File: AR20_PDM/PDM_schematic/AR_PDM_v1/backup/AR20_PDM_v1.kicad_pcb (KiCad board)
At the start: 2 copper layers, 118 x 112 mm, 243 parts, among them J1 S_T_?, J2 1-776163-1, K1 DIPxx-1Cxx-51x, K2 DIPxx-1Cxx-51x, Q1 BTS50025-1TAD, Q10 N_FET, Q11 N_FET, Q12 N_FET, Q13 N_FET, Q14 N_FET, Q15 N_FET, Q16 N_FET, Q17 N_FET, Q18 N_FET, Q2 BTS50025-1TAD, Q3 BTS50025-1TAD, Q4 BTS50025-1TAD, Q5 BTS50025-1TAD, Q6 BTS50025-1TAD, Q7 BTS50025-1TAD, Q8 N_FET, Q9 N_FET, SW1 SW_DIP_x07, SW2 SW_Push, U1 ACM_2020, U10 INA233, U11 INA233, U12 TCA6424ARGJR, U13 Fet-P, U14 Fet-P, U15 Fet-P, U16 Fet-P, U17 Fet-P, U18 Fet-P, U19 Fet-P, U2 INA233, U20 Fet-P, U21 Fet-P, U22 Fet-P, U23 Fet-P, U24 Fet-P, U25 Fet-P, U26 Fet-P, U27 Fet-P, U28 Fet-P, U29 Fet-P, U3 INA233, U30 Fet-P, U31 Fet-P, U4 INA233, U5 INA233, U6 INA233, U7 INA233, U8 INA233, U9 INA233

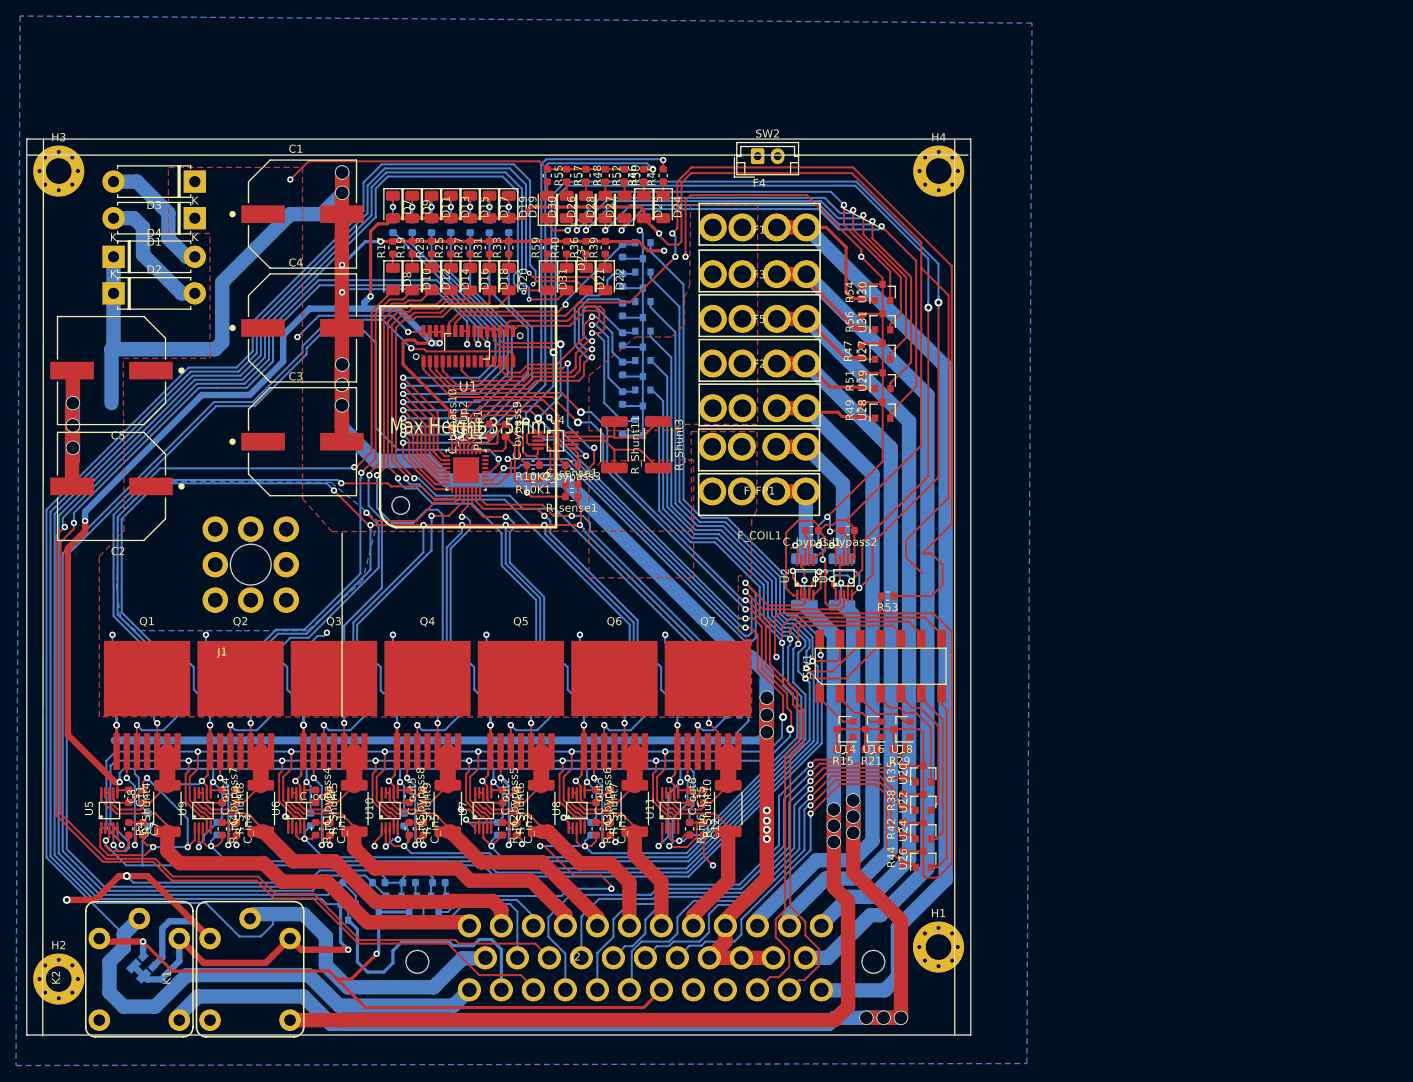
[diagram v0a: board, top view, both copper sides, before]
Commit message: Finilizing the desing, some few missing components
- Increased the size to accommodate mounting holes
- Fixed wrong p mos pin out, due to wrong schematics drawing
- Done alot of tweeeks 
- Button connector still missing.
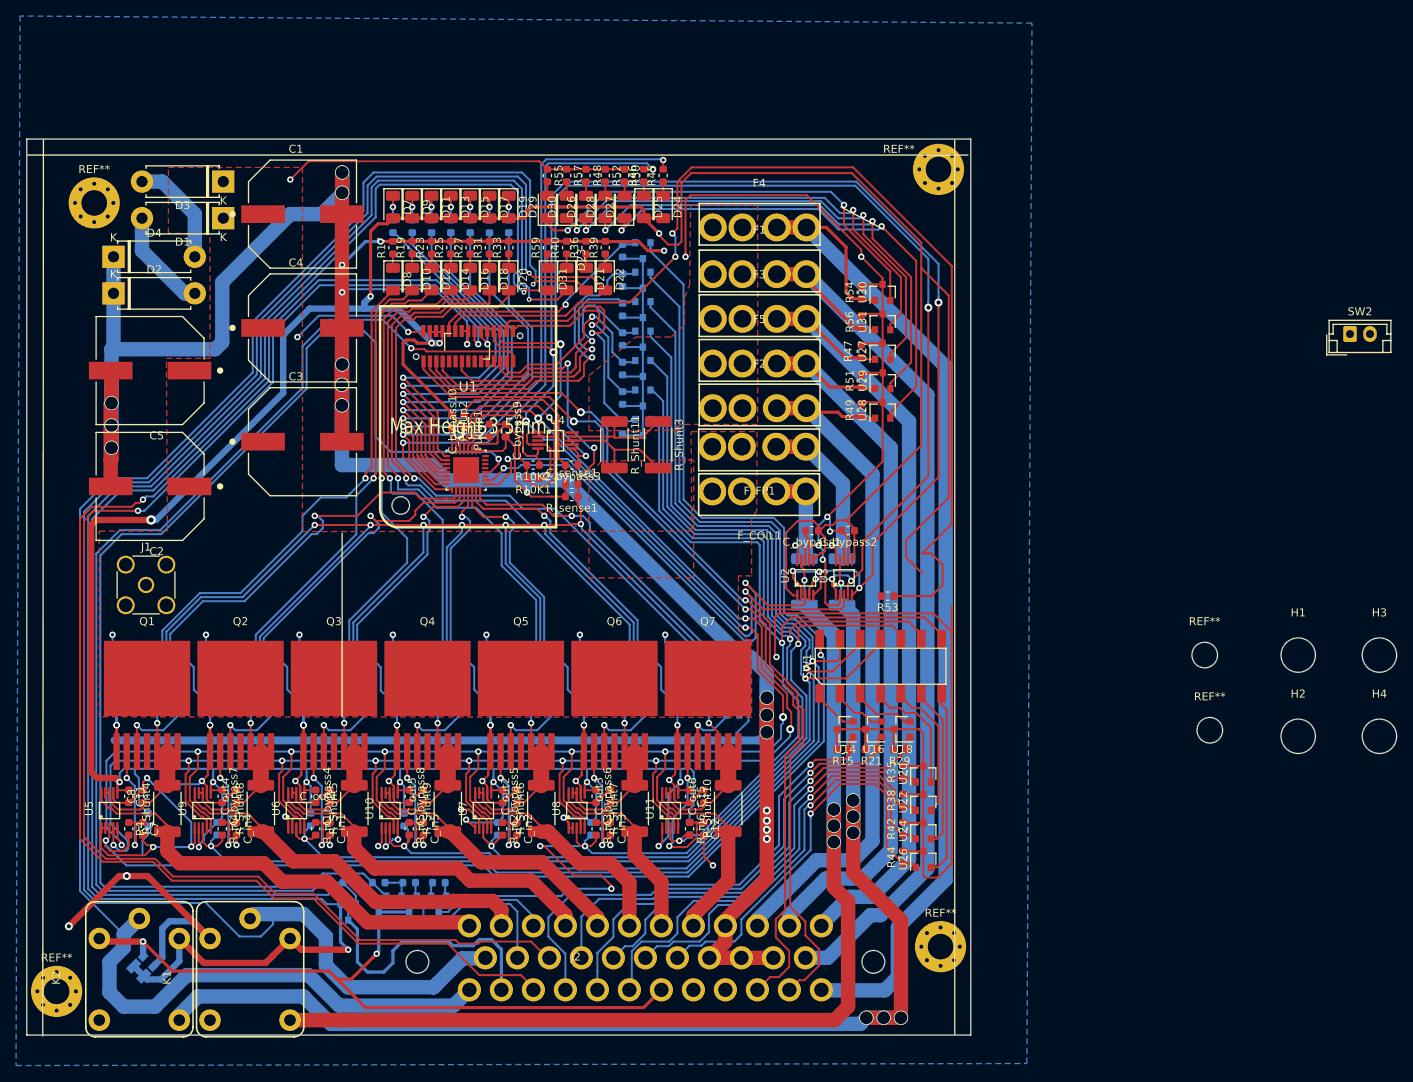
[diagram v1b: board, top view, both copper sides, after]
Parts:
- added REF**: MountingHole_3.2mm_M3_Pad_Via, MountingHole:MountingHole_3.2mm_M3_Pad_Via, F.Cu at (42.3, 44.3)
- added REF**: MountingHole_3.2mm_M3_Pad_Via, MountingHole:MountingHole_3.2mm_M3_Pad_Via, F.Cu at (147.8, 40.1)
- added REF**: MountingHole_3.2mm_M3_Pad_Via, MountingHole:MountingHole_3.2mm_M3_Pad_Via, F.Cu at (148.1, 137.3)
- added REF**: MountingHole_3.2mm_M3_PDM, AR_PDM_v1:MountingHole_3.2mm_M3, F.Cu at (181.7, 110.2)
- added REF**: MountingHole_3.2mm_M3_PDM, AR_PDM_v1:MountingHole_3.2mm_M3, F.Cu at (181.1, 100.8)
- added REF**: MountingHole_3.2mm_M3_Pad_Via, MountingHole:MountingHole_3.2mm_M3_Pad_Via, F.Cu at (37.6, 142.9)
- H1, H2, H3, H4: footprint MountingHole:MountingHole_3.2mm_M3_Pad_Via -> MountingHole:MountingHole_4.3mm_M4
- J1: value S_T_? -> High_Curret_terminal; footprint AR_PDM_v1:Wurth 74655095R Screw Post -> Connector_Coaxial:SMA_Amphenol_132291_Vertical
- moved H3 175.8 mm to (202.9, 100.8)
- moved H2 157.9 mm to (192.8, 111.0)
- moved H4 89.6 mm to (202.9, 111.0)
- moved SW2 77.3 mm to (199.3, 60.7)
- moved H1 57.9 mm to (192.8, 100.8)
- moved J1 8.86 mm to (48.8, 92.1)
- moved C2 4.83 mm to (49.3, 79.8)
- moved C5 4.83 mm to (49.3, 65.3)
- moved D1 3.56 mm to (58.4, 46.2)
- moved D3 3.56 mm to (58.4, 41.7)
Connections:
- H1 pad 1: GND -> (no net)
- H2 pad 1: GND -> (no net)
- H3 pad 1: GND -> (no net)
- H4 pad 1: GND -> (no net)
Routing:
- net GND: track 1115.7 -> 1061.1 mm, vias 63 -> 62
- net MOS_SENSE_ALL: track 261.9 -> 239.6 mm
- net P1_MOS_SENSE_Select: track 75.5 -> 53.5 mm
- net P1_Shunt: track 106.2 -> 92.2 mm
- net COIL_INJECTOR_OUT: track 218.4 -> 212.4 mm
- net SHUTDOWN_IN: track 212.8 -> 207.4 mm
- net Shutdown_Led: track 223.6 -> 218.2 mm
- net FUEL_PUMP_OUT: track 222.1 -> 217.0 mm
- net P4_Shunt: track 91.3 -> 86.6 mm
- net P2_MOS_IN: track 167.0 -> 170.4 mm
- net P5_MOS_IN: track 126.8 -> 130.3 mm
- net P3_MOS_IN: track 152.5 -> 155.9 mm
- net P6_MOS_IN: track 153.3 -> 156.7 mm
- net ACM_Shutdown_Circuit: track 149.7 -> 146.3 mm
- net P7_MOS_IN: track 97.5 -> 100.7 mm
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- removed copper zone on B.Cu, net V+12V
